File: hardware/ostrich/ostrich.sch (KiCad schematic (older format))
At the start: 54 parts, among them J1 CONN_01X40, J2 CONN_01X08, J3 CONN_01X06, J4 CONN_01X10, J5 CONN_01X08, J6 CONN_01X10, J7 Micro_SD_Card_CD, J8 CONN_01X13, J9 CONN_01X04, M1 ESP-11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

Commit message: Fixed SD slot orientation and diode footprint
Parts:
- C1, C10, C11, C12, C13, C14, C15, C16, C2, C3, C4, C5, C6, C7, C8, C9: symbol C -> device:C
- D1, D2: footprint Diodes_SMD:D_0805 -> Diodes_SMD:D_1206; symbol D_Schottky -> device:D_Schottky
- D3, D4, D5, D6: symbol LED -> device:LED
- J1: symbol CONN_01X40 -> conn1:CONN_01X40
- J2, J5: symbol CONN_01X08 -> conn1:CONN_01X08
- J3: symbol CONN_01X06 -> conn1:CONN_01X06
- J4, J6: symbol CONN_01X10 -> conn1:CONN_01X10
- J7: symbol Micro_SD_Card_CD -> micro_sd_card_cd:Micro_SD_Card_CD
- J8: symbol CONN_01X13 -> conn1:CONN_01X13
- J9: symbol CONN_01X04 -> conn1:CONN_01X04
- M1: symbol ESP-11 -> esp-11:ESP-11
- M2, M3, M4, M5: symbol CONN_01X01 -> conn1:CONN_01X01
- P1: symbol USB_OTG -> conn1:USB_OTG
- Q1: symbol Q_NMOS_GSD -> device:Q_NMOS_GSD
- R1, R2, R3, R4, R5, R6: symbol R -> device:R
- R10, R7, R8, R9: value 1KR -> 100R; symbol R -> device:R
- SW1, SW2: symbol SW_SPST -> switches1:SW_SPST
- U1: symbol LD1117S33TR_WTAB -> ld1117s33tr_wtab:LD1117S33TR_WTAB
- U2: symbol STM32F745ZETx -> stm321:STM32F745ZETx
- U3: symbol IS42S16160G -> is42s16160g:IS42S16160G
- Y1: symbol Crystal_Small -> device:Crystal_Small
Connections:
- wire segments 374 -> 434

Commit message: Added Vbus and rearranged digital pins
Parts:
- C1, C10, C11, C12, C13, C14, C15, C16, C2, C3, C4, C5, C6, C7, C8, C9: symbol device:C -> ostrich-rescue:C-device
- D1, D2: symbol device:D_Schottky -> ostrich-rescue:D_Schottky-device
- D3, D4, D5, D6: symbol device:LED -> ostrich-rescue:LED-device
- Q1: symbol device:Q_NMOS_GSD -> ostrich-rescue:Q_NMOS_GSD-device
- R1, R10, R2, R3, R4, R5, R6, R7, R8, R9: symbol device:R -> ostrich-rescue:R-device
- Y1: symbol device:Crystal_Small -> ostrich-rescue:Crystal_Small-device
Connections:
- net labels added: PA7
- wire segments 434 -> 436

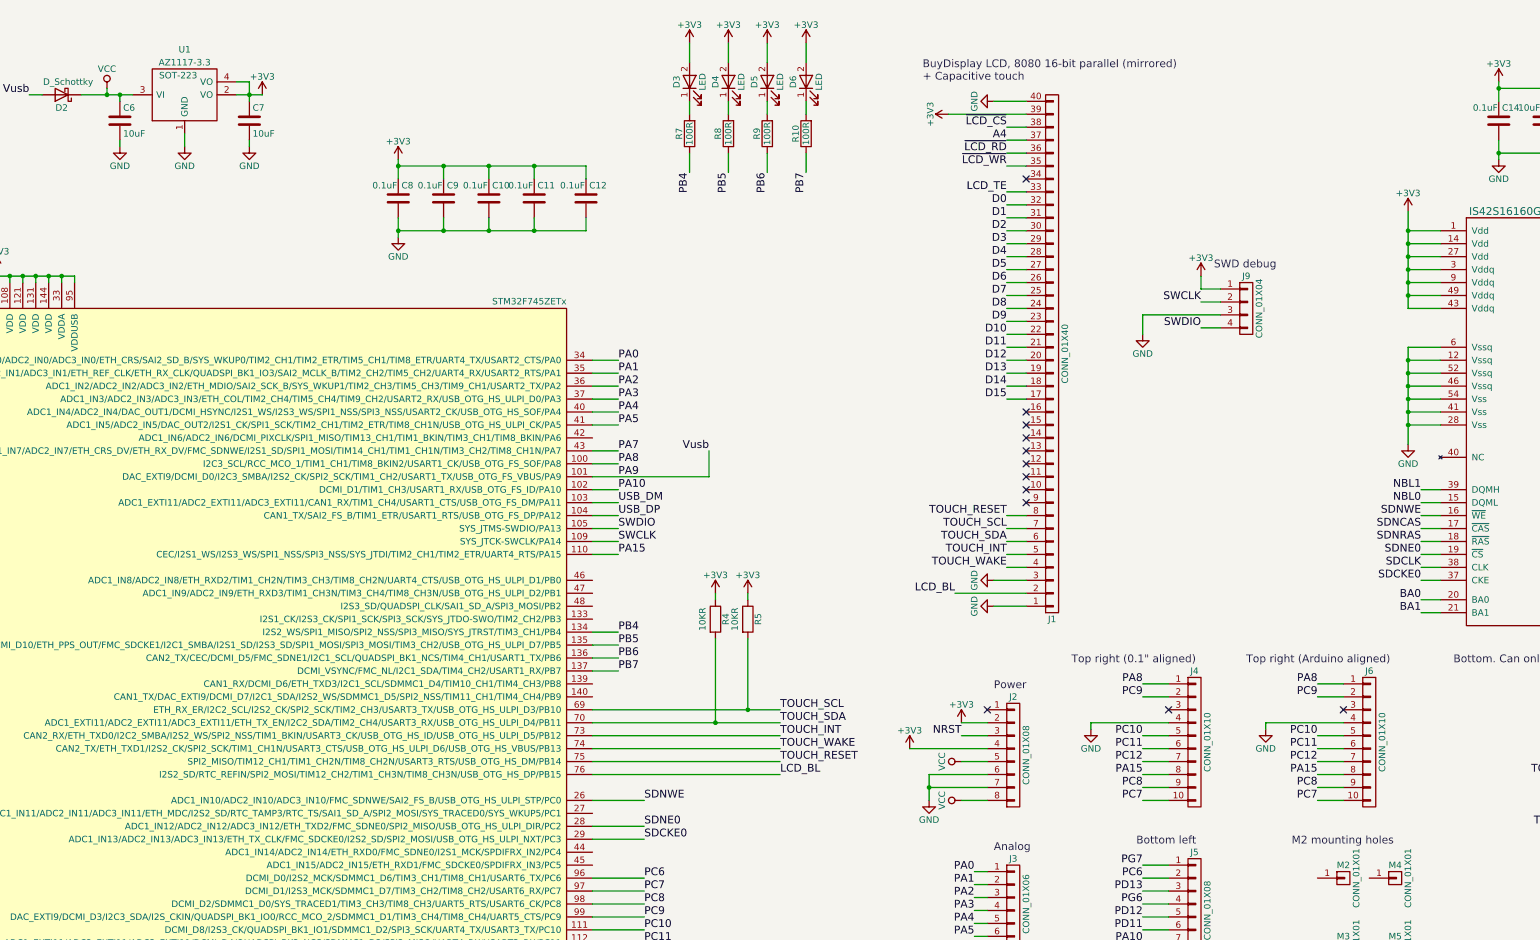
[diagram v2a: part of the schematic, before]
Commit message: Updated footprint table for KiCad 5, removed 0.1 inch aligned connector, and added all SWD pins
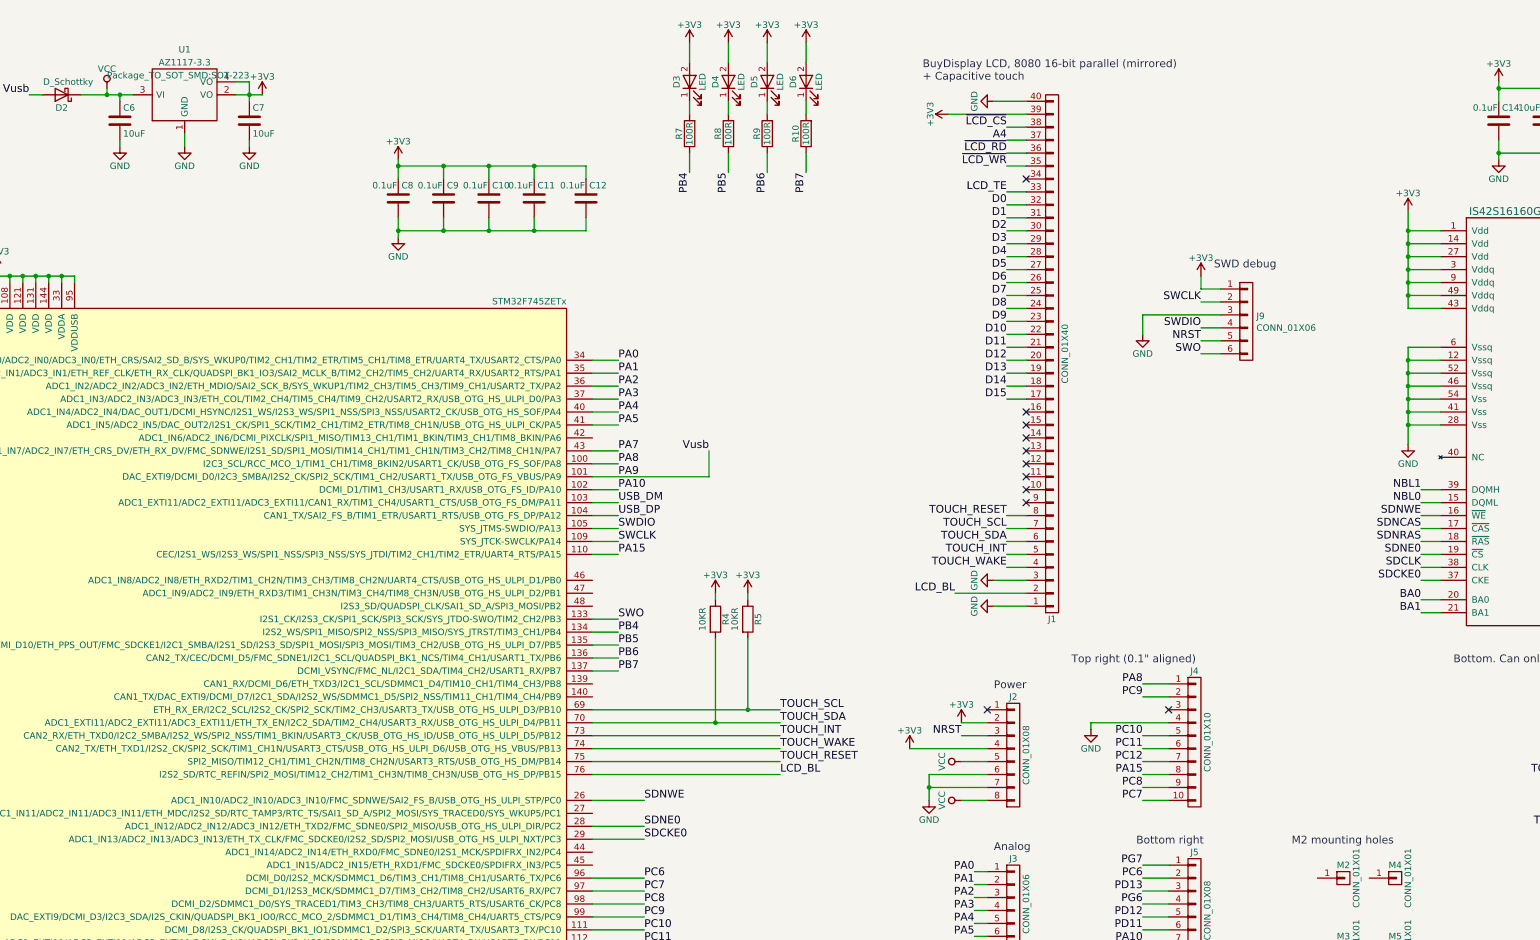
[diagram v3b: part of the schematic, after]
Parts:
- removed J6: CONN_01X10, Pin_Headers:Pin_Header_Straight_1x10_Pitch2.54mm, symbol conn1:CONN_01X10
- removed J9: CONN_01X04, Pin_Headers:Pin_Header_Straight_1x04_Pitch2.54mm, symbol conn1:CONN_01X04
- added J9: CONN_01X06, Connector_PinHeader_2.54mm:PinHeader_1x06_P2.54mm_Vertical, symbol conn1:CONN_01X06
- J4: footprint Pin_Headers:Pin_Header_Straight_1x10_Pitch2.54mm -> Connector_PinHeader_2.54mm:PinHeader_1x10_P2.54mm_Vertical
- U1: footprint SOT-223 -> Package_TO_SOT_SMD:SOT-223
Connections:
- net +3V3: now also J9.1 (P1)
- net GND: now also J9.3 (P3)
- net NRST: now also J9.5 (P5)
- net SWCLK: now also J9.2 (P2)
- net SWDIO: now also J9.4 (P4)
- net SWO: now reaches U2.133 (I2S1_CK/I2S3_CK/SPI1_SCK/SPI3_SCK/SYS_JTDO-SWO/TIM2_CH2/PB3)
- net SWO: now also J9.6 (P6)
- no-connect marks 15 -> 14
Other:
- note added: "Bottom right"
- note removed: "Bottom left"
- note removed: "Top right (Arduino aligned)"
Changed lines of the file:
@@
 PA5
-$Comp
-L conn1:CONN_01X10 J4
-U 1 1 58A50C2C
-P 16500 6350
-F 0 "J4" H 16500 6900 50  0000 C CNN
-F 1 "CONN_01X10" V 16600 6350 50  0000 C CNN
-F 2 "Pin_Headers:Pin_Header_Straight_1x10_Pitch2.54mm" H 16500 6350 50  0001 C CNN
-F 3 "" H 16500 6350 50  0001 C CNN
-	1    16500 6350
-	1    0    0    -1
-$EndComp
 $Comp
 L conn1:CONN_01X08 J5
@@
 Text Label 2450 5800 2    60   ~ 0
 PG7
-Text Label 16100 6800 2    60   ~ 0
-PC7
-Text Label 16100 6700 2    60   ~ 0
-PC8
-Text Label 16100 6600 2    60   ~ 0
-PA15
-Text Label 16100 6500 2    60   ~ 0
-PC12
-Text Label 16100 6400 2    60   ~ 0
-PC11
-Text Label 16100 6300 2    60   ~ 0
-PC10
-Text Label 16100 6000 2    60   ~ 0
-PC9
-Text Label 16100 5900 2    60   ~ 0
-PA8
-NoConn ~ 16300 6100
-$Comp
-L ostrich-rescue:GND-power #PWR048
-U 1 1 58A55075
-P 15700 6250
-F 0 "#PWR048" H 15700 6000 50  0001 C CNN
-F 1 "GND" H 15700 6100 50  0000 C CNN
-F 2 "" H 15700 6250 50  0000 C CNN
-F 3 "" H 15700 6250 50  0000 C CNN
-	1    15700 6250
-	1    0    0    -1
-$EndComp
 Text Label 12250 7500 0    60   ~ 0
 PC7
@@
 PA8
 $Comp
-L conn1:CONN_01X10 J6
-U 1 1 58A57186
-P 17850 6350
-F 0 "J6" H 17850 6900 50  0000 C CNN
-F 1 "CONN_01X10" V 17950 6350 50  0000 C CNN
-F 2 "Pin_Headers:Pin_Header_Straight_1x10_Pitch2.54mm" H 17850 6350 50  0001 C CNN
-F 3 "" H 17850 6350 50  0001 C CNN
-	1    17850 6350
-	1    0    0    -1
-$EndComp
-Text Label 17450 6800 2    60   ~ 0
-PC7
-Text Label 17450 6700 2    60   ~ 0
-PC8
-Text Label 17450 6600 2    60   ~ 0
-PA15
-Text Label 17450 6500 2    60   ~ 0
-PC12
-Text Label 17450 6400 2    60   ~ 0
-PC11
-Text Label 17450 6300 2    60   ~ 0
-PC10
-Text Label 17450 6000 2    60   ~ 0
-PC9
-Text Label 17450 5900 2    60   ~ 0
-PA8
-$Comp
-L ostrich-rescue:GND-power #PWR054
-U 1 1 58A5728A
-P 17050 6250
-F 0 "#PWR054" H 17050 6000 50  0001 C CNN
-F 1 "GND" H 17050 6100 50  0000 C CNN
-F 2 "" H 17050 6250 50  0000 C CNN
-F 3 "" H 17050 6250 50  0000 C CNN
-	1    17050 6250
-	1    0    0    -1
-$EndComp
-NoConn ~ 17650 6100
-$Comp
 L ld1117s33tr_wtab:LD1117S33TR_WTAB U1
 U 1 1 58A579EF
@@
 F 0 "U1" H 8700 1800 50  0000 C CNN
 F 1 "AZ1117-3.3" H 8700 1700 50  0000 C CNN
-F 2 "SOT-223" H 8650 1600 50  0000 C CNN
+F 2 "Package_TO_SOT_SMD:SOT-223" H 8650 1600 50  0000 C CNN
 F 3 "" H 8700 1400 50  0000 C CNN
 	1    8700 1400
@@
 	9100 1250 9200 1250
 Wire Wire Line
-	17050 6200 17650 6200
-Wire Wire Line
-	17050 6250 17050 6200
-Wire Wire Line
-	17650 6800 17450 6800
-Wire Wire Line
-	17450 6700 17650 6700
-Wire Wire Line
-	17650 6600 17450 6600
-Wire Wire Line
-	17450 6500 17650 6500
-Wire Wire Line
-	17650 6400 17450 6400
-Wire Wire Line
-	17450 6300 17650 6300
-Wire Wire Line
-	17650 6000 17450 6000
-Wire Wire Line
-	17450 5900 17650 5900
-Wire Wire Line
 	12250 8000 11850 8000
 Wire Wire Line
@@
 Wire Wire Line
 	12050 4200 11850 4200
-Wire Wire Line
-	15700 6200 16300 6200
-Wire Wire Line
-	15700 6250 15700 6200
-Wire Wire Line
-	16300 6800 16100 6800
-Wire Wire Line
-	16100 6700 16300 6700
-Wire Wire Line
-	16300 6600 16100 6600
-Wire Wire Line
-	16100 6500 16300 6500
-Wire Wire Line
-	16300 6400 16100 6400
-Wire Wire Line
-	16100 6300 16300 6300
-Wire Wire Line
-	16300 6000 16100 6000
-Wire Wire Line
-	16100 5900 16300 5900
 Wire Wire Line
 	2450 5800 2650 5800
@@
 	2500 8800 2650 8800
 Text Notes 16050 7150 0    60   ~ 0
-Bottom left
-Text Notes 15550 5750 0    60   ~ 0
-Top right (0.1" aligned)
-Text Notes 16900 5750 0    60   ~ 0
-Top right (Arduino aligned)
-$Comp
-L conn1:CONN_01X04 J9
-U 1 1 58B10013
-P 16900 3000
-F 0 "J9" H 16900 3250 50  0000 C CNN
-F 1 "CONN_01X04" V 17000 3000 50  0000 C CNN
-F 2 "Pin_Headers:Pin_Header_Straight_1x04_Pitch2.54mm" H 16900 3000 50  0001 C CNN
-F 3 "" H 16900 3000 50  0001 C CNN
-	1    16900 3000
-	1    0    0    -1
-$EndComp
+Bottom right
 Text Notes 16650 2700 0    60   ~ 0
 SWD debug
@@
 	12050 4100 11850 4100
 $Comp
-L ostrich-rescue:GND-power #PWR?
+L ostrich-rescue:GND-power #PWR0101
 U 1 1 5CF53B47
 P 16100 8000
-F 0 "#PWR?" H 16100 7750 50  0001 C CNN
+F 0 "#PWR0101" H 16100 7750 50  0001 C CNN
 F 1 "GND" H 16100 7850 50  0000 C CNN
 F 2 "" H 16100 8000 50  0000 C CNN
@@
 	1    0    0    -1
 $EndComp
+Text Label 12050 5400 0    60   ~ 0
+SWO
+Wire Wire Line
+	12050 5400 11850 5400
+$Comp
+L conn1:CONN_01X06 J9
+U 1 1 5CEB4AE1
+P 16900 3100
+F 0 "J9" H 16978 3141 50  0000 L CNN
+F 1 "CONN_01X06" H 16978 3050 50  0000 L CNN
+F 2 "Connector_PinHeader_2.54mm:PinHeader_1x06_P2.54mm_Vertical" H 16900 3100 50  0001 C CNN
+F 3 "" H 16900 3100 50  0001 C CNN
+	1    16900 3100
+	1    0    0    -1
+$EndComp
+Text Label 16550 3250 2    60   ~ 0
+NRST
+Wire Wire Line
+	16550 3250 16700 3250
+Text Label 16550 3350 2    60   ~ 0
+SWO
+Wire Wire Line
+	16550 3350 16700 3350
+Text Notes 15550 5750 0    60   ~ 0
+Top right (0.1" aligned)
+Wire Wire Line
+	16100 5900 16300 5900
+Wire Wire Line
+	16300 6000 16100 6000
+Wire Wire Line
+	16100 6300 16300 6300
+Wire Wire Line
+	16300 6400 16100 6400
+Wire Wire Line
+	16100 6500 16300 6500
+Wire Wire Line
+	16300 6600 16100 6600
+Wire Wire Line
+	16100 6700 16300 6700
+Wire Wire Line
+	16300 6800 16100 6800
+Wire Wire Line
+	15700 6250 15700 6200
+Wire Wire Line
+	15700 6200 16300 6200
+$Comp
+L ostrich-rescue:GND-power #PWR048
+U 1 1 58A55075
+P 15700 6250
+F 0 "#PWR048" H 15700 6000 50  0001 C CNN
+F 1 "GND" H 15700 6100 50  0000 C CNN
+F 2 "" H 15700 6250 50  0000 C CNN
+F 3 "" H 15700 6250 50  0000 C CNN
+	1    15700 6250
+	1    0    0    -1
+$EndComp
+NoConn ~ 16300 6100
+Text Label 16100 5900 2    60   ~ 0
+PA8
+Text Label 16100 6000 2    60   ~ 0
+PC9
+Text Label 16100 6300 2    60   ~ 0
+PC10
+Text Label 16100 6400 2    60   ~ 0
+PC11
+Text Label 16100 6500 2    60   ~ 0
+PC12
+Text Label 16100 6600 2    60   ~ 0
+PA15
+Text Label 16100 6700 2    60   ~ 0
+PC8
+Text Label 16100 6800 2    60   ~ 0
+PC7
+$Comp
+L conn1:CONN_01X10 J4
+U 1 1 58A50C2C
+P 16500 6350
+F 0 "J4" H 16500 6900 50  0000 C CNN
+F 1 "CONN_01X10" V 16600 6350 50  0000 C CNN
+F 2 "Connector_PinHeader_2.54mm:PinHeader_1x10_P2.54mm_Vertical" H 16500 6350 50  0001 C CNN
+F 3 "" H 16500 6350 50  0001 C CNN
+	1    16500 6350
+	1    0    0    -1
+$EndComp
